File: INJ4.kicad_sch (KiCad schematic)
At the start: 20 parts, among them Q1 AOD4184A, Q2 AOD4184A, Q3 AOD4184A, Q4 AOD4184A

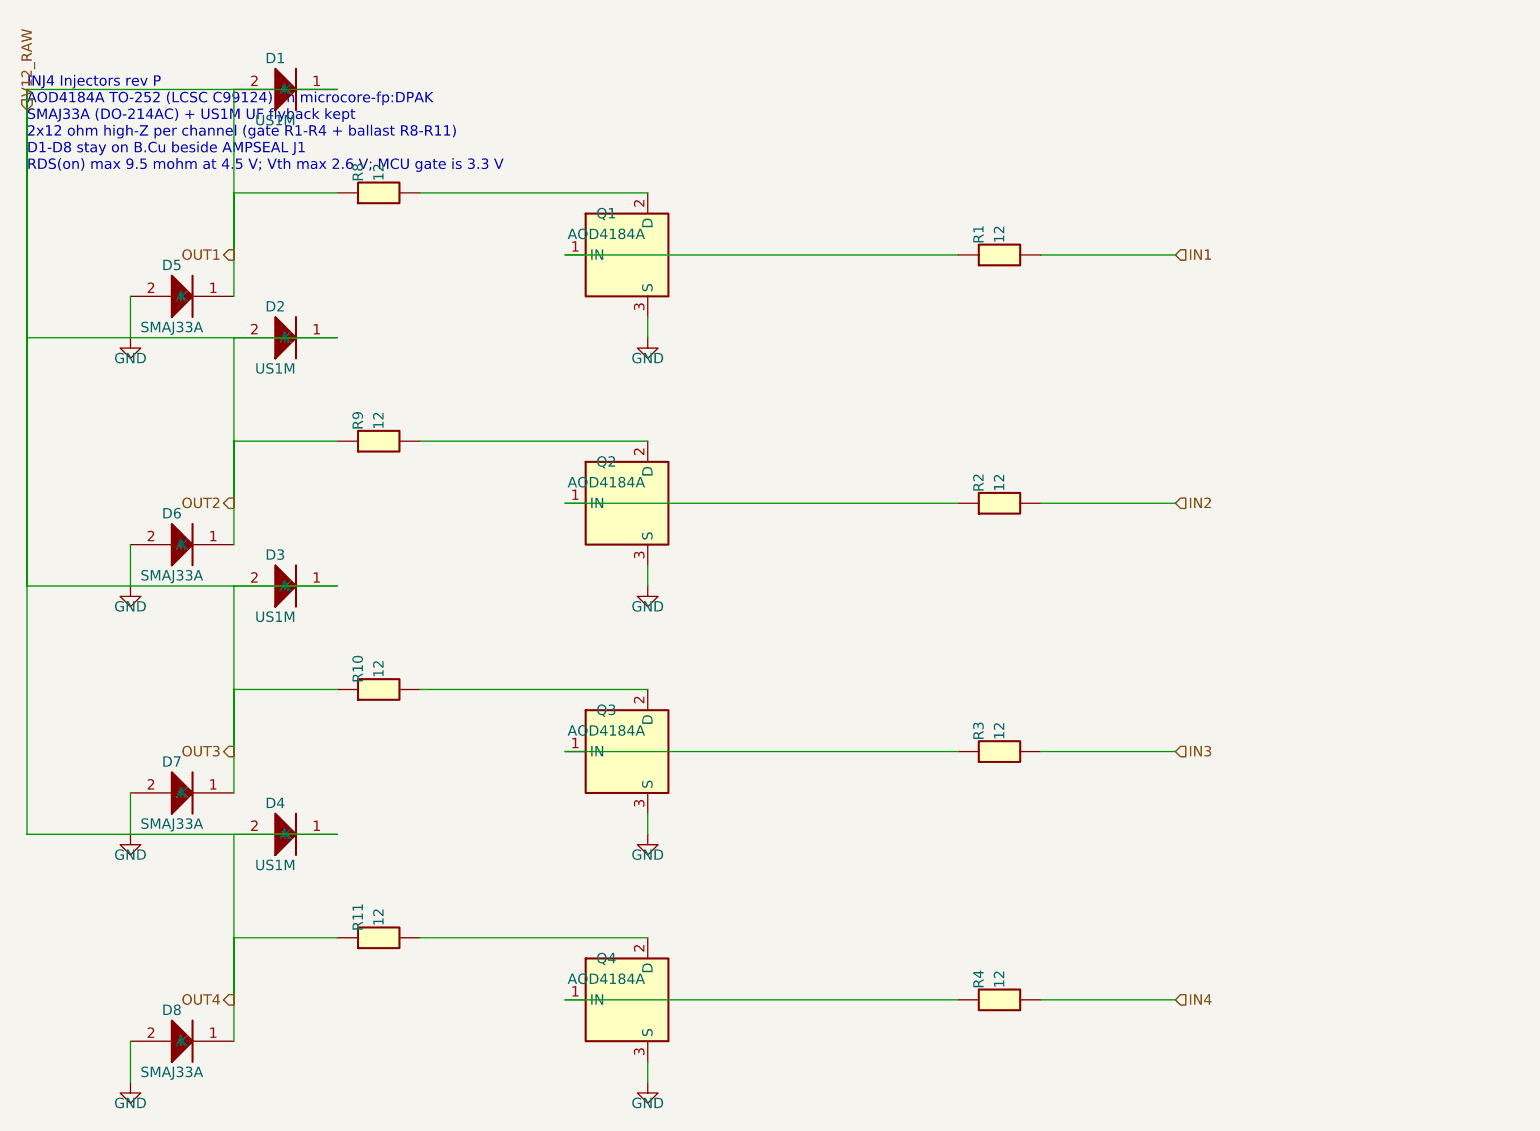
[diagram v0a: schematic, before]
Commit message: Rev q: NCE4080K (C191380) plus SLM27524 gate drivers on V12_RAW
Restore Q1-Q7 to NCE4080K and insert four SLM27524CA-DG drivers so the
STM32 GPIO no longer drives the FET gates. Seven channels are used; the
spare input is tied to GND. LS clamps and the rev p short fixes stay.

Co-authored-by: Quintin <quintinbannink42@users.noreply.github.com>
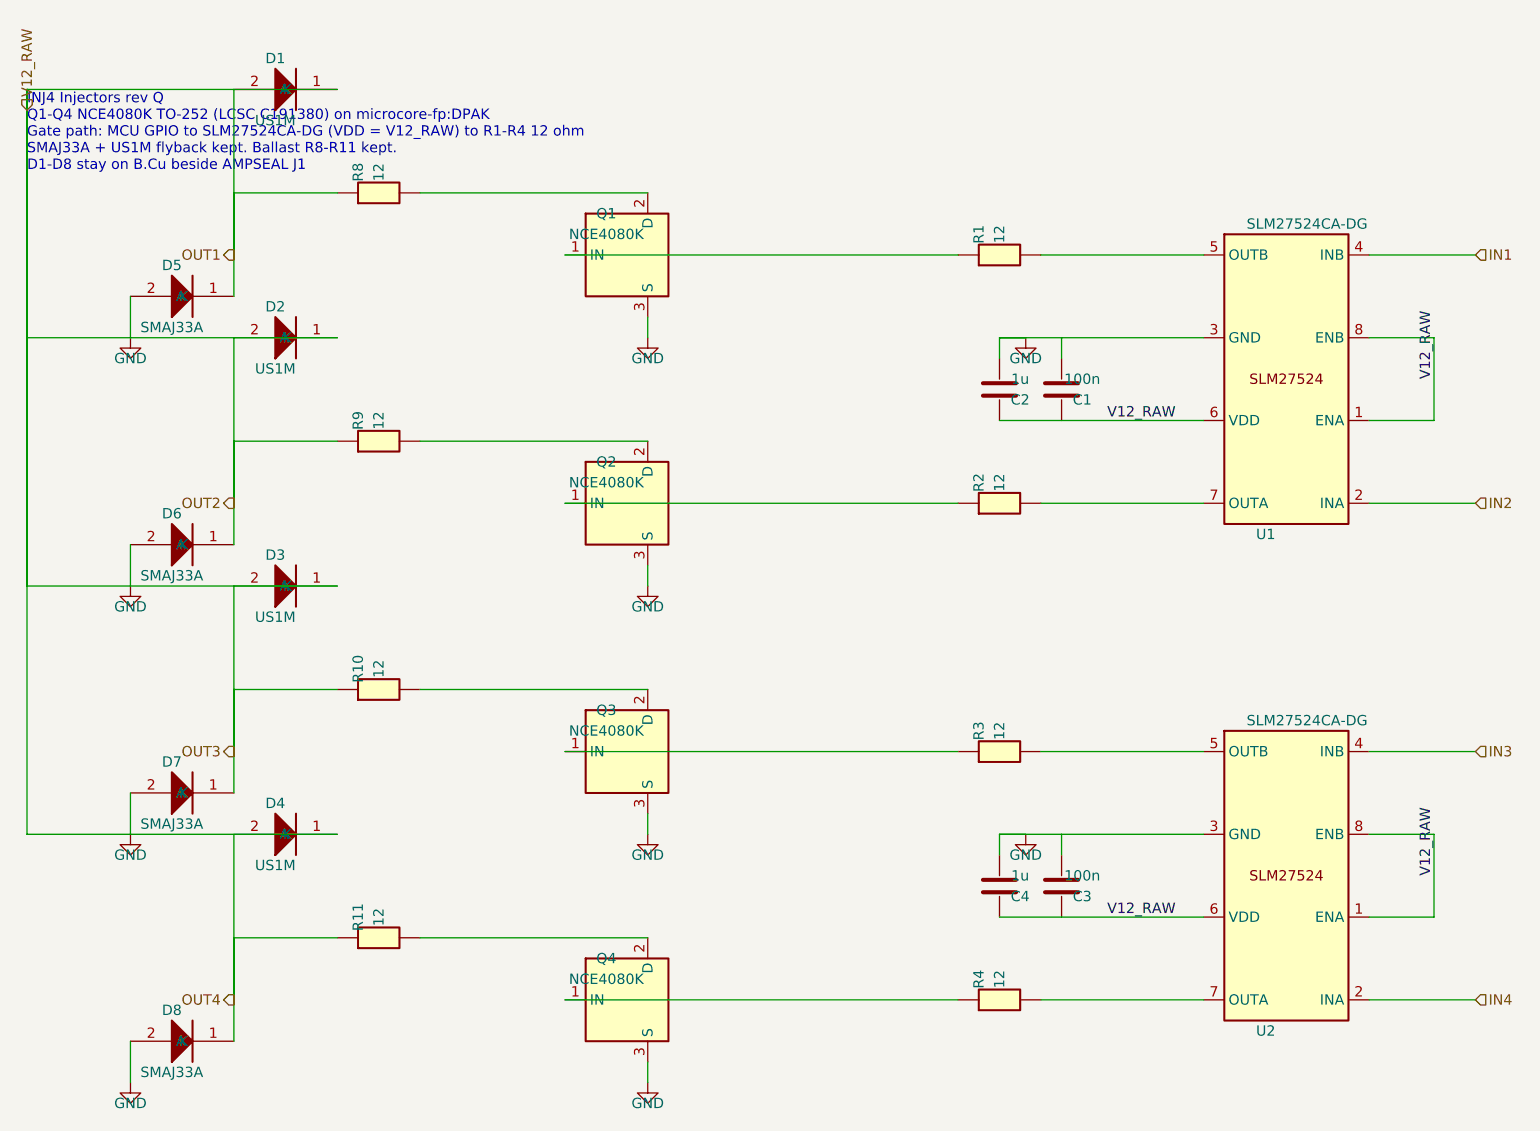
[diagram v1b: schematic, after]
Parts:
- added C1, C3: 100n, microcore-fp:C0603, symbol microcore:C
- added C2, C4: 1u, microcore-fp:C0603, symbol microcore:C
- added U1, U2: SLM27524CA-DG, microcore-fp:SOIC-8, symbol microcore:SLM27524
- Q1, Q2, Q3, Q4: value AOD4184A -> NCE4080K
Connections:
- net GND: now also C1.1, C2.1, C3.1, C4.1, U1.3 (GND), U2.3 (GND)
- net IN1: now also U1.4 (INB); no longer R1.2
- net IN2: now also U1.2 (INA); no longer R2.2
- net IN3: now also U2.4 (INB); no longer R3.2
- net IN4: now also U2.2 (INA); no longer R4.2
- net V12_RAW: now also C1.2, C2.2, C3.2, C4.2, U1.1 (ENA), U1.6 (VDD), U1.8 (ENB), U2.1 (ENA), U2.6 (VDD), U2.8 (ENB)
- new net: R3.2, U2.5 (OUTB)
- new net: R4.2, U2.7 (OUTA)
- new net: R1.2, U1.5 (OUTB)
- new net: R2.2, U1.7 (OUTA)
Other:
- note added: "INJ4 Injectors rev Q Q1-Q4 NCE4080K TO-252 (LCSC C191380) on microcore-fp:DPAK Gate path: MCU GPIO to SLM27524CA-DG (VDD = V12_RAW) to R1-R4 12 ohm SMAJ33A + US1M flyback kept. Ballast R8-R11 kept. D1-D8 stay on B.Cu beside AMPSEAL J1"
- note removed: "INJ4 Injectors rev P AOD4184A TO-252 (LCSC C99124) on microcore-fp:DPAK SMAJ33A (DO-214AC) + US1M UF flyback kept 2x12 ohm high-Z per channel (gate R1-R4 + ballast R8-R11) D1-D8 stay on B.Cu beside AMPSEAL J1 RDS(on) max 9.5 mohm at 4.5 V; Vth max 2.6 V; MCU gate is 3.3 V"
